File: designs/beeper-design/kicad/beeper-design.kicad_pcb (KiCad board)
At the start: 4 copper layers, 27.5 x 19 mm, 99 parts

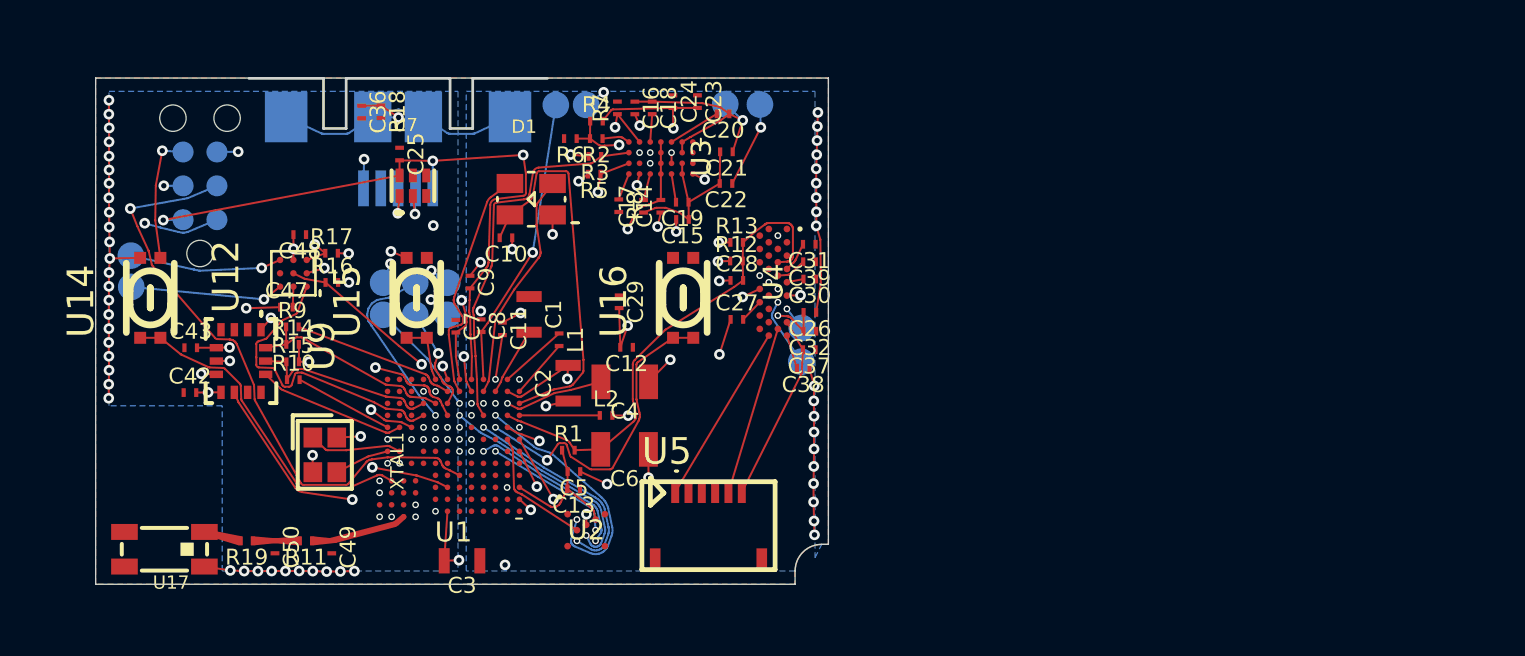
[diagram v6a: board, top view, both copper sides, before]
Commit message: exported, yet XTALM32p keeps disappearing
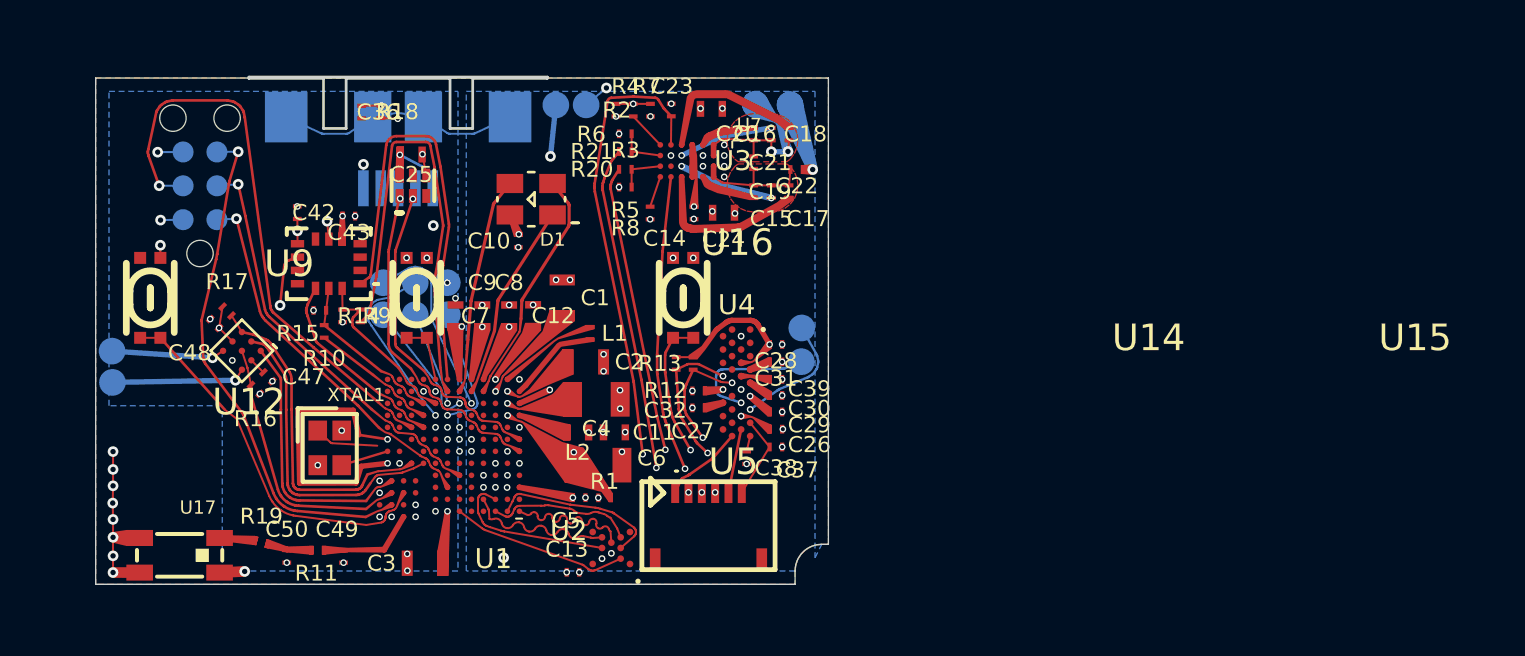
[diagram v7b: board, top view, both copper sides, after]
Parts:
- removed the C24 at (147.4, 99.4)
- removed the C6 at (145.6, 112.4)
- removed the D1 at (142.1, 103.0)
- removed the TP1 at (127.1, 106.3)
- added ?: , beeper-design:dummy9, F.Cu at (146.6, 100.4)
- added ?: , beeper-design:dummy10, F.Cu at (138.3, 110.6)
- added ?: , beeper-design:dummy11, F.Cu at (137.3, 109.6)
- added ?: , beeper-design:dummy12, F.Cu at (150.5, 109.8)
- added ?: , beeper-design:dummy13, F.Cu at (150.7, 110.2)
- added ?: , beeper-design:dummy14, F.Cu at (148.5, 100.5)
- added ?: , beeper-design:dummy15, F.Cu at (147.6, 100.7)
- added ?: , beeper-design:dummy16, F.Cu at (148.5, 101.6)
- added ?: , beeper-design:dummy17, F.Cu at (148.7, 102.7)
- added ?: , beeper-design:dummy18, F.Cu at (141.4, 112.4)
- added ?: , beeper-design:dummy19, F.Cu at (137.7, 109.6)
- added ?: , beeper-design:dummy20, F.Cu at (150.7, 109.3)
- added ?: , beeper-design:dummy21, F.Cu at (137.4, 113.0)
- added ?: , beeper-design:dummy22, F.Cu at (136.1, 113.3)
- added ?: , beeper-design:dummy23, F.Cu at (138.8, 113.6)
- added ?: , beeper-design:dummy24, F.Cu at (136.6, 111.7)
- added ?: , beeper-design:dummy25, F.Cu at (135.8, 116.2)
- added ?: , beeper-design:dummy26, F.Cu at (136.9, 115.6)
- added ?: , beeper-design:dummy27, F.Cu at (134.7, 116.2)
- added ?: , beeper-design:dummy28, F.Cu at (139.5, 109.3)
- added ?: , beeper-design:dummy29, F.Cu at (150.7, 99.7)
- added ?: , beeper-design:dummy30, F.Cu at (148.5, 100.0)
- added ?: , beeper-design:dummy31, F.Cu at (144.3, 116.8)
- added ?: , beeper-design:dummy32, F.Cu at (143.8, 114.4)
- added ?: , beeper-design:dummy33, F.Cu at (144.5, 114.4)
- added ?: , beeper-design:dummy34, F.Cu at (143.8, 115.6)
- added ?: , beeper-design:dummy35, F.Cu at (142.6, 114.1)
- added ?: , beeper-design:dummy36, F.Cu at (149.7, 102.7)
- added ?: , beeper-design:dummy37, F.Cu at (148.6, 102.4)
- added ?: , beeper-design:dummy38, F.Cu at (142.6, 111.6)
- added ?: , beeper-design:dummy39, F.Cu at (136.6, 110.4)
- added ?: , beeper-design:dummy40, F.Cu at (137.8, 111.5)
- added ?: , beeper-design:dummy41, F.Cu at (139.2, 113.3)
- added ?: , beeper-design:dummy42, F.Cu at (136.3, 111.1)
- added ?: , beeper-design:dummy43, F.Cu at (138.2, 109.7)
- added ?: , beeper-design:dummy44, F.Cu at (141.4, 112.0)
- added ?: , beeper-design:dummy45, F.Cu at (140.3, 109.2)
- added ?: , beeper-design:dummy46, F.Cu at (138.9, 109.8)
- added ?: , beeper-design:dummy47, F.Cu at (150.9, 103.6)
- added ?: , beeper-design:dummy49, F.Cu at (131.1, 115.8)
- added ?: , beeper-design:dummy50, F.Cu at (133.4, 116.2)
- added ?: , beeper-design:dummy51, F.Cu at (132.6, 116.1)
- added ?: , beeper-design:dummy52, F.Cu at (141.5, 104.0)
- added ?: , beeper-design:dummy53, F.Cu at (142.2, 110.4)
- added ?: , beeper-design:dummy54, F.Cu at (137.8, 111.1)
- added ?: , beeper-design:dummy55, F.Cu at (136.4, 109.8)
- added ?: , beeper-design:dummy56, F.Cu at (141.3, 110.8)
- added ?: , beeper-design:dummy57, F.Cu at (142.8, 110.6)
- added ?: , beeper-design:dummy58, F.Cu at (135.0, 104.2)
- added ?: , beeper-design:dummy59, F.Cu at (141.4, 111.2)
- added ?: , beeper-design:dummy61, F.Cu at (150.5, 108.8)
- added ?: , beeper-design:dummy62, F.Cu at (148.6, 108.5)
- added ?: , beeper-design:dummy63, F.Cu at (144.3, 113.4)
- added ?: , beeper-design:dummy64, F.Cu at (151.0, 100.2)
- added ?: , beeper-design:dummy66, F.Cu at (141.5, 108.8)
- added ?: , beeper-design:dummy67, F.Cu at (150.7, 110.8)
- added ?: , beeper-design:dummy68, F.Cu at (148.2, 102.2)
- added ?: , beeper-design:dummy6, F.Cu at (136.1, 114.5)
- added ?: , beeper-design:dummy69, F.Cu at (148.1, 101.6)
- added ?: , beeper-design:dummy71, F.Cu at (148.1, 102.0)
- added ?: , beeper-design:dummy72, F.Cu at (140.2, 108.8)
- added ?: , beeper-design:dummy73, F.Cu at (148.1, 101.2)
- added ?: , beeper-design:dummy74, F.Cu at (142.8, 108.8)
- added ?: , beeper-design:dummy75, F.Cu at (127.1, 115.8)
- added ?: , beeper-design:dummy76, F.Cu at (152.1, 100.6)
- added ?: , beeper-design:dummy77, F.Cu at (152.5, 101.9)
- added ?: , beeper-design:dummy78, F.Cu at (149.6, 110.7)
- added ?: , beeper-design:dummy7, F.Cu at (149.9, 100.5)
- added ?: , beeper-design:dummy80, F.Cu at (139.3, 108.8)
- added ?: , beeper-design:dummy81, F.Cu at (150.5, 111.5)
- added ?: , beeper-design:dummy82, F.Cu at (143.1, 109.2)
- added ?: , beeper-design:dummy83, F.Cu at (136.7, 113.7)
- added ?: , beeper-design:dummy84, F.Cu at (136.1, 114.1)
- added ?: , beeper-design:dummy85, F.Cu at (140.8, 110.0)
- added ?: , beeper-design:dummy86, F.Cu at (142.4, 108.5)
- added ?: , beeper-design:dummy87, F.Cu at (137.2, 114.3)
- added ?: , beeper-design:dummy8, F.Cu at (148.6, 100.8)
- added ?: , beeper-design:dummy89, F.Cu at (141.3, 110.3)
- added ?: , beeper-design:dummy90, F.Cu at (142.7, 109.6)
- added ?: , beeper-design:dummy91, F.Cu at (138.8, 115.9)
- added ?: , beeper-design:dummy92, F.Cu at (136.4, 114.7)
- added ?: , beeper-design:dummy93, F.Cu at (149.4, 102.4)
- added ?: , beeper-design:dummy94, F.Cu at (140.4, 110.1)
- added ?: , beeper-design:dummy95, F.Cu at (141.7, 107.7)
- added ?: , beeper-design:dummy96, F.Cu at (149.0, 110.8)
- added ?: , beeper-design:dummy98, F.Cu at (140.9, 108.8)
- added C1: 22u, beeper-design:Pkg0603, F.Cu at (143.3, 106.7)
- added C2: 22u, beeper-design:Pkg0603_1, F.Cu at (144.1, 109.2)
- added C37: 1u, beeper-design:Pkg0201_18, F.Cu at (151.3, 112.3)
- added C48: 1u, beeper-design:Pkg0201_33, F.Cu at (130.2, 107.7)
- added R16: 8K2, beeper-design:Pkg0201_40, F.Cu at (131.7, 110.2)
- added R20: 0R, beeper-design:Pkg0201, F.Cu at (145.6, 101.9)
- added R21: 0R, beeper-design:Pkg0201_8, F.Cu at (145.6, 101.3)
- added R7: 10K, beeper-design:Pkg0201_12, F.Cu at (147.4, 99.7)
- added R8: 1K, beeper-design:Pkg0201_16, F.Cu at (146.6, 103.6)
- added TP5: ~, beeper-design:SMD_TESTPT, B.Cu at (136.5, 106.2)
- added TP6: ~, beeper-design:SMD_TESTPT, B.Cu at (137.7, 106.2)
- added U16: ~, beeper-design:LP_2, F.Cu at (147.8, 106.8)
- added U2: ~, beeper-design:WLCSP_12, F.Cu at (145.1, 116.1)
- ?: renamed from U2; value ~ -> (none); footprint beeper-design:WLCSP_12 -> beeper-design:dummy48
- ?: renamed from TP6; value ~ -> (none); footprint beeper-design:SMD_TESTPT -> beeper-design:dummy60; moved to F.Cu
- ?: renamed from TP5; value ~ -> (none); footprint beeper-design:SMD_TESTPT -> beeper-design:dummy65; moved to F.Cu
- ?: renamed from R16; value 8K2 -> (none); footprint beeper-design:Pkg0201_31 -> beeper-design:dummy70
- ?: renamed from R7; value 10K -> (none); footprint beeper-design:Pkg0201_23 -> beeper-design:dummy79
- ?: renamed from C2; value 22u -> (none); footprint beeper-design:Pkg0603_1 -> beeper-design:dummy88
- ?: renamed from C37; value 2.2u -> (none); footprint beeper-design:Pkg0201_39 -> beeper-design:dummy97
- C10: footprint beeper-design:Pkg0201_12 -> beeper-design:Pkg0201_27
- C11: value 2.2u -> 10u; footprint beeper-design:Pkg0201_5 -> beeper-design:Pkg0402_6
- C12: value 2.2u -> 10u; footprint beeper-design:Pkg0201_25 -> beeper-design:Pkg0402_5
- C13: value 2.2u -> 1u; footprint beeper-design:Pkg0201_28 -> beeper-design:Pkg0201_29
- C14: footprint beeper-design:Pkg0201 -> beeper-design:Pkg0201_20
- C15: value 2.2u -> 470n; footprint beeper-design:Pkg0201_50 -> beeper-design:Pkg0201_23
- C16: value 2.2u -> 470n; footprint beeper-design:Pkg0201_9 -> beeper-design:Pkg0201_30
- C17: value 2.2u -> 22n; footprint beeper-design:Pkg0201_22 -> beeper-design:Pkg0201_36
- C18: value 2.2u -> 22n; footprint beeper-design:Pkg0201_36 -> beeper-design:Pkg0201_44
- C19: value 2.2u -> 10n; footprint beeper-design:Pkg0201_49 -> beeper-design:Pkg0201_2
- C20: value 2.2u -> 10n; footprint beeper-design:Pkg0201_7 -> beeper-design:Pkg0201_11
- C21: value 2.2u -> 270p; footprint beeper-design:Pkg0201_20 -> beeper-design:Pkg0201_17
- C22: value 2.2u -> 10n; footprint beeper-design:Pkg0201_33 -> beeper-design:Pkg0201_22
- C23: value 2.2u -> 10u; footprint beeper-design:Pkg0201_48 -> beeper-design:Pkg0402_4
- C24: renamed from C1; value 22u -> 4.7u; footprint beeper-design:Pkg0603 -> beeper-design:Pkg0402_7
- C25: value 2.2u -> 4.7u; footprint beeper-design:Pkg0201_18 -> beeper-design:Pkg0402_8
- C26: value 2.2u -> 1u; footprint beeper-design:Pkg0201_34 -> beeper-design:Pkg0201_43
- C27: value 2.2u -> 100n; footprint beeper-design:Pkg0201_53 -> beeper-design:Pkg0201_46
- C28: value 2.2u -> 1u; footprint beeper-design:Pkg0201_42 -> beeper-design:Pkg0201_38
- C29: value 2.2u -> 1u; footprint beeper-design:Pkg0201_24 -> beeper-design:Pkg0201_13
- C30: value 2.2u -> 1u; footprint beeper-design:Pkg0201_8 -> beeper-design:Pkg0201_31
- C31: value 2.2u -> 1u; footprint beeper-design:Pkg0201_21 -> beeper-design:Pkg0201_35
- C32: value 2.2u -> 1u; footprint beeper-design:Pkg0201_11 -> beeper-design:Pkg0201_6
- C36: value 2.2u -> 100n; footprint beeper-design:Pkg0201_30 -> beeper-design:Pkg0201_7
- C38: value 2.2u -> 1u; footprint beeper-design:Pkg0201_51 -> beeper-design:Pkg0201_24
- C39: value 2.2u -> 1u; footprint beeper-design:Pkg0201_47 -> beeper-design:Pkg0201_1
- C42: value 2.2u -> 100n; footprint beeper-design:Pkg0201_43 -> beeper-design:Pkg0201_34
- C43: value 2.2u -> 100n; footprint beeper-design:Pkg0201_3 -> beeper-design:Pkg0201_41
- C47: value 2.2u -> 1u; footprint beeper-design:Pkg0201_4 -> beeper-design:Pkg0201_26
- C49: value 2.2u -> 1p; footprint beeper-design:Pkg0201_37 -> beeper-design:Pkg0201_5
- C5: value 2.2u -> 100n; footprint beeper-design:Pkg0201_1 -> beeper-design:Pkg0201_39
- C50: value 2.2u -> 1p; footprint beeper-design:Pkg0201_2 -> beeper-design:Pkg0201_15
- C6: renamed from R8; value 1K -> 47u; footprint beeper-design:Pkg0201_38 -> beeper-design:Pkg0805
- C7: value 2.2u -> 10u; footprint beeper-design:Pkg0201_26 -> beeper-design:Pkg0402
- C8: value 2.2u -> 10u; footprint beeper-design:Pkg0201_41 -> beeper-design:Pkg0402_1
- C9: value 2.2u -> 10u; footprint beeper-design:Pkg0201_54 -> beeper-design:Pkg0402_2
- D1: renamed from C48; value 2.2u -> ~; footprint beeper-design:Pkg0201_16 -> beeper-design:LP_5
- L1: footprint beeper-design:Pkg0201_32 -> beeper-design:Pkg0201_21
- L2: value 470n -> 1u; footprint beeper-design:Pkg0201_46 -> beeper-design:Pkg0402_3
- R1: footprint beeper-design:Pkg0201_19 -> beeper-design:Pkg0201_14
- R10: footprint beeper-design:Pkg0201_44 -> beeper-design:Pkg0201_9
- R11: footprint beeper-design:Pkg0201_45 -> beeper-design:Pkg0201_10
- R12, R13: footprint beeper-design:Pkg0201_29 -> beeper-design:Pkg0201_28
- R14, R15: footprint beeper-design:Pkg0201_14 -> beeper-design:Pkg0201_42
- R17: footprint beeper-design:Pkg0201_31 -> beeper-design:Pkg0201_40
- R18: footprint beeper-design:Pkg0201_17 -> beeper-design:Pkg0201_47
- R19: footprint beeper-design:Pkg0201_13 -> beeper-design:Pkg0201_19
- R2: footprint beeper-design:Pkg0201_15 -> beeper-design:Pkg0201_25
- R3: footprint beeper-design:Pkg0201_10 -> beeper-design:Pkg0201_4
- R4: footprint beeper-design:Pkg0201_40 -> beeper-design:Pkg0201_37
- R5: footprint beeper-design:Pkg0201_52 -> beeper-design:Pkg0201_45
- R6: footprint beeper-design:Pkg0201_27 -> beeper-design:Pkg0201_32
- R9: footprint beeper-design:Pkg0201_35 -> beeper-design:Pkg0201_3
- TP1: renamed from U16; footprint beeper-design:LP_2 -> beeper-design:SMD_TESTPT; moved to B.Cu
- moved TP1 21.7 mm to (126.4, 109.9), turned to 180 degrees
- moved ? 20.2 mm to (148.9, 102.0)
- moved ? 13.4 mm to (148.9, 101.2), turned to 0 degrees
- moved ? 13.0 mm to (147.8, 103.0)
- moved ? 11.5 mm to (141.1, 107.5), turned to 0 degrees
- moved ? 11.2 mm to (149.0, 110.2), turned to 0 degrees
- moved C6 9.77 mm to (144.6, 113.0), turned to 270 degrees
- moved ? 9.02 mm to (136.2, 115.2), turned to 0 degrees
- moved ? 8.95 mm to (137.8, 110.6)
- moved D1 8.79 mm to (142.1, 103.0), turned to 0 degrees
- moved C24 8.24 mm to (149.3, 103.6), turned to 270 degrees
- moved ? 8.17 mm to (142.9, 112.5), turned to 0 degrees
- moved C42 7.86 mm to (133.3, 103.6), turned to 0 degrees
- moved ? 7.76 mm to (136.6, 109.6)
- moved C43 7.72 mm to (135.3, 103.7), turned to 270 degrees
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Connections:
- net board-io_qsen-i3c_sda renamed mcu_sda2
- net codec-pdm-net_clk renamed board-io_clk
- net codec-pdm-net_data renamed board-io_data
- net mcu_mcu-button1_gpio renamed mcu1_gpio1
- net mcu_mcu-dbg-m33_swdclk renamed mcu_swdclk
- net mcu_mcu-dbg-m33_swdio renamed mcu_swdio
- net mcu_mcu-etm_data1 renamed mcu_data1
- net mcu_mcu-etm_data2 renamed mcu_data2
- net mcu_mcu-etm_data3 renamed mcu_data3
- net mcu_q-spi_sdo renamed mcu_sdo
- C24 pad 2: V12 -> RECT
- C3 pad 2: V14 -> V14RF
- C6 pad 1: AD -> GND
- C6 pad 2: GND -> VDD1P8P
- D1 pad 1: GND -> board-io_r
- D1 pad 2: VDDSYS -> VLED
- J1 pad 3: mcu_conn-uart_rx -> mcu_rx
- J1 pad 6: mcu_mcu-uart_tx -> mcu_tx
- R10 pad 1: board-io_qsen-i3c_scl -> mcu_scl
- R10 pad 2: mcu_q-spi_sck -> mcu_sck
- R12 pad 1: codec-i2c-net_sda -> mcu_sda
- R13 pad 1: codec-i2c-net_scl -> mcu_scl2
- R15 pad 1: board-io_qsen-i3c_scl -> mcu_scl
- R17 pad 1: mcu_hap-i2c_scl -> mcu_scl1
- R3 pad 1: mcu_mcu-wpwr1_gpio -> EN2
- R5 pad 1: mcu_mcu-wpwr0_gpio -> EN1
- U1 pad A1: (no net) -> mcu_sdio0
- U1 pad A2: (no net) -> mcu_sdio1
- U1 pad A3: (no net) -> mcu_sdio2
- U1 pad A6: (no net) -> mcu_cs1
- U1 pad A7: V14 -> V14RF
- U1 pad B1: codec-i2c-net_scl -> (no net)
- U1 pad B11: (no net) -> mcu_tx
- U1 pad B3: (no net) -> mcu_sdio3
- U1 pad B4: (no net) -> mcu_sck1
- U1 pad C10: (no net) -> mcu0_gpio1
- U1 pad C11: (no net) -> mcu_sda1
- U1 pad C3: (no net) -> mcu_scl2
- U1 pad C4: (no net) -> mcu2_gpio1
- U1 pad D11: mcu_mcu-button0_gpio -> mcu0_gpio
- U1 pad D2: (no net) -> mcu2_gpio
- U1 pad D4: (no net) -> mcu_sda
- U1 pad E1: (no net) -> mcu1_gpio2
- U1 pad E10: (no net) -> mcu_scl1
- U1 pad E3: (no net) -> mcu0_gpio2
- U1 pad E9: (no net) -> mcu1_gpio
- U1 pad F2: (no net) -> mcu3_gpio
- U1 pad F3: mcu_mcu-mem_sdio3 -> (no net)
- U1 pad F4: mcu_mcu-mem_sck -> (no net)
- U1 pad G10: mcu_hap-i2c_scl -> (no net)
- U1 pad G2: mcu_mcu-mem_sdio1 -> (no net)
- U1 pad G8: mcu_conn-uart_rx -> (no net)
- U1 pad G9: mcu_mcu-uart_tx -> (no net)
- U1 pad H10: mcu_q-spi_sdi -> mcu_rx
- U1 pad H11: mcu_q-spi_cs -> (no net)
- U1 pad H12: mcu_q-spi_sck -> (no net)
- U1 pad H2: codec-i2c-net_sda -> (no net)
- U1 pad H3: mcu_mcu-button2_gpio -> (no net)
- U1 pad H4: mcu_mcu-mem_sdio2 -> (no net)
- U1 pad H9: mcu_hap-gpio1_gpio -> mcu_cs
- U1 pad J3: mcu_mcu-mem_cs -> (no net)
- U1 pad J4: mcu_mcu-wpwr1_gpio -> (no net)
- U1 pad J5: mcu_mcu-wpwr3_gpio -> (no net)
- U1 pad J6: mcu_mcu-mem_sdio0 -> (no net)
- U1 pad J8: mcu_mcu-etm_data0 -> mcu_data0
- U1 pad J9: mcu_hap-gpio0_gpio -> mcu_sck
- U1 pad K3: mcu_mcu-wpwr2_gpio -> (no net)
- U1 pad K4: mcu_mcu-wpwr0_gpio -> (no net)
- U1 pad K5: mcu_mcu-etm_clk -> mcu_clk
- U1 pad K9: board-io_qsen-i3c_scl -> mcu_scl
- U1 pad L2: V14 -> V14RF
- U1 pad L4: board-io_rgb_b -> board-io_b
- U1 pad L5: board-io_rgb_r -> board-io_r
- U1 pad L6: board-io_rgb_g -> board-io_g
- U1 pad M7: mcu_hap-i2c_sda -> mcu_sdi
- U12 pad A1: mcu_hap-gpio0_gpio -> mcu0_gpio
- U12 pad B1: mcu_hap-gpio1_gpio -> mcu1_gpio
- U12 pad B2: mcu_hap-i2c_sda -> mcu_sda1
- U12 pad C1: mcu_hap-i2c_scl -> mcu_scl1
- U14 pad A: mcu_mcu-button0_gpio -> mcu0_gpio1
- U14 pad A1: mcu_mcu-button0_gpio -> mcu0_gpio1
- U3 pad F1: mcu_mcu-wpwr3_gpio -> mcu3_gpio
- U3 pad F4: mcu_mcu-wpwr2_gpio -> mcu2_gpio1
- U3 pad G2: mcu_mcu-wpwr1_gpio -> EN2
- U3 pad G3: mcu_mcu-wpwr0_gpio -> EN1
- U4 pad C9: codec-i2c-net_sda -> mcu_sda
- U4 pad D8: codec-i2c-net_scl -> mcu_scl2
- U9 pad 1: mcu_q-spi_sdi -> mcu_sdi
- U9 pad 12: mcu_q-spi_cs -> mcu_cs
- U9 pad 13: board-io_qsen-i3c_scl -> mcu_scl
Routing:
- net GND: track 53.7 -> 25.5 mm, vias 101 -> 98
- net VDDSYS: track 6.88 -> 31.8 mm, vias 7 -> 6
- net mcu3_gpio: track 0.00 -> 22.5 mm, vias 0 -> 2
- net mcu_rx: track 0.00 -> 20.9 mm, vias 0 -> 1
- net mcu2_gpio1: track 0.00 -> 19.1 mm, vias 0 -> 2
- net mcu_tx: track 0.00 -> 18.2 mm, vias 0 -> 1
- net mcu0_gpio2: track 0.00 -> 17.9 mm, vias 0 -> 2
- net mcu1_gpio2: track 0.00 -> 17.4 mm, vias 0 -> 2
- net mcu_sdi: track 0.00 -> 16.5 mm
- net codec-i2c-net_scl: track 15.6 -> 0.00 mm, vias 3 -> 0
- net mcu_conn-uart_rx: track 15.2 -> 0.00 mm, vias 2 -> 0
- net VDD3P0: track 25.4 -> 10.9 mm
- net mcu_mcu-wpwr3_gpio: track 14.2 -> 0.00 mm, vias 2 -> 0
- net mcu_mcu-wpwr1_gpio: track 14.2 -> 0.00 mm
- net mcu_mcu-uart_tx: track 14.1 -> 0.00 mm, vias 2 -> 0
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- added copper zone on F.Cu, net AC1
- added copper zone on F.Cu, net AC2
- added copper zone on In2.Cu, net GND
- added copper zone on In2.Cu, net VBAT
- added copper zone on In2.Cu, net VBUS
- added copper zone on In2.Cu, net VDD1P8
- added copper zone on In2.Cu, net VDD1P8P
- added copper zone on In2.Cu, net VDD3P0
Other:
- net class BGA added: clearance 0.065, trace_width 0.075, via_dia 0.015, via_drill 0.15
- net class Default added: clearance 0.0625, trace_width 0.075, via_dia 0.015, via_drill 0.15
- net class RF added: clearance 0.0625, trace_width 0.221435, via_dia 0.015, via_drill 0.15
- rule pad_to_mask_clearance: 0 -> 0.051

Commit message: fixed up pours, keepout regions
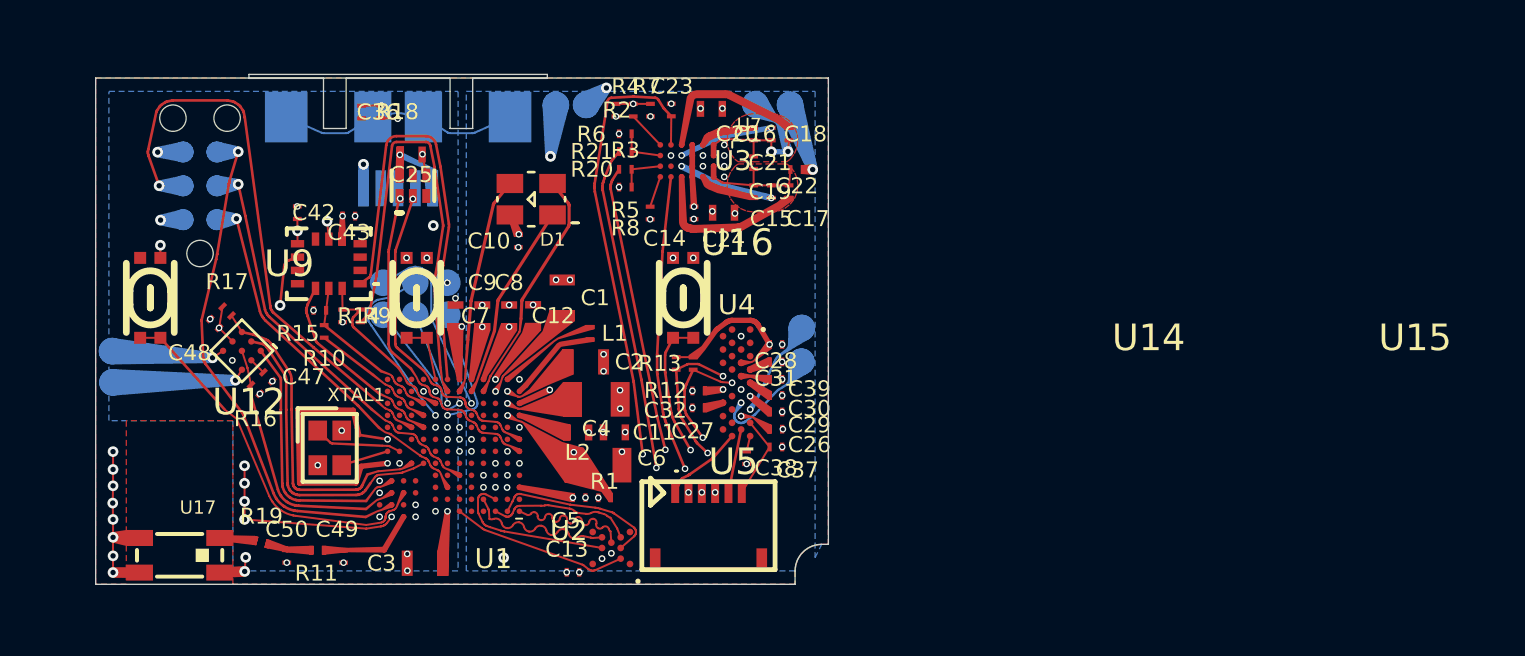
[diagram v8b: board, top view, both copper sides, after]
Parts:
- removed the ? at (148.5, 101.6)
- removed the ? at (143.8, 115.6)
- removed the ? at (139.2, 113.3)
- removed the ? at (133.4, 116.2)
- added ?: , beeper-design:dummy103, F.Cu at (136.4, 109.8)
- added ?: , beeper-design:dummy110, F.Cu at (148.6, 108.5)
- added ?: , beeper-design:dummy104, F.Cu at (141.3, 110.8)
- added ?: , beeper-design:dummy107, F.Cu at (141.4, 111.2)
- added ?: , beeper-design:dummy108, F.Cu at (142.9, 112.5)
- added ?: , beeper-design:dummy101, F.Cu at (151.5, 109.2)
- added ?: , beeper-design:dummy112, F.Cu at (151.0, 100.2)
- added ?: , beeper-design:dummy105, F.Cu at (142.8, 110.6)
- added ?: , beeper-design:dummy106, F.Cu at (135.0, 104.2)
- added ?: , beeper-design:dummy102, F.Cu at (137.8, 111.1)
- added ?: , beeper-design:dummy111, F.Cu at (144.3, 113.4)
- added ?: , beeper-design:dummy109, F.Cu at (150.5, 108.8)
- added ?: , beeper-design:dummy99, F.Cu at (141.5, 104.0)
- added ?: , beeper-design:dummy100, F.Cu at (142.2, 110.4)
- added ?: , beeper-design:dummy113, F.Cu at (148.9, 101.2)
- added C27: 100n, beeper-design:Pkg0201_12, F.Cu at (148.4, 110.9)
- added R13: 8K2, beeper-design:Pkg0201_42, F.Cu at (147.5, 109.2)
- added R14: 8K2, beeper-design:Pkg0201_8, F.Cu at (135.0, 107.4)
- added U3: ~, beeper-design:LP_1, F.Cu at (148.1, 101.6)
- ?: renamed from R13; value 8K2 -> (none); footprint beeper-design:Pkg0201_28 -> beeper-design:dummy34
- ?: renamed from C27; value 100n -> (none); footprint beeper-design:Pkg0201_46 -> beeper-design:dummy50
- ?: renamed from R14; value 8K2 -> (none); footprint beeper-design:Pkg0201_42 -> beeper-design:dummy41
- ?: renamed from U3; value ~ -> (none); footprint beeper-design:LP_6 -> beeper-design:dummy16
- C10: footprint beeper-design:Pkg0201_27 -> beeper-design:Pkg0201_41
- C11: footprint beeper-design:Pkg0402_6 -> beeper-design:Pkg0402_8
- C12: footprint beeper-design:Pkg0402_5 -> beeper-design:Pkg0402_7
- C13: footprint beeper-design:Pkg0201_29 -> beeper-design:Pkg0201_43
- C14: footprint beeper-design:Pkg0201_20 -> beeper-design:Pkg0201_34
- C15: footprint beeper-design:Pkg0201_23 -> beeper-design:Pkg0201_37
- C16: footprint beeper-design:Pkg0201_30 -> beeper-design:Pkg0201_44
- C17: footprint beeper-design:Pkg0201_36 -> beeper-design:Pkg0201_2
- C18: footprint beeper-design:Pkg0201_44 -> beeper-design:Pkg0201_10
- C19: footprint beeper-design:Pkg0201_2 -> beeper-design:Pkg0201_16
- C20: footprint beeper-design:Pkg0201_11 -> beeper-design:Pkg0201_25
- C21: footprint beeper-design:Pkg0201_17 -> beeper-design:Pkg0201_31
- C22: footprint beeper-design:Pkg0201_22 -> beeper-design:Pkg0201_36
- C23: footprint beeper-design:Pkg0402_4 -> beeper-design:Pkg0402_6
- C24: footprint beeper-design:Pkg0402_7 -> beeper-design:Pkg0402
- C25: footprint beeper-design:Pkg0402_8 -> beeper-design:Pkg0402_1
- C26: footprint beeper-design:Pkg0201_43 -> beeper-design:Pkg0201_9
- C28: footprint beeper-design:Pkg0201_38 -> beeper-design:Pkg0201_4
- C29: footprint beeper-design:Pkg0201_13 -> beeper-design:Pkg0201_27
- C30: footprint beeper-design:Pkg0201_31 -> beeper-design:Pkg0201_45
- C31: footprint beeper-design:Pkg0201_35 -> beeper-design:Pkg0201_1
- C32: footprint beeper-design:Pkg0201_6 -> beeper-design:Pkg0201_20
- C36: footprint beeper-design:Pkg0201_7 -> beeper-design:Pkg0201_21
- C37: footprint beeper-design:Pkg0201_18 -> beeper-design:Pkg0201_32
- C38: footprint beeper-design:Pkg0201_24 -> beeper-design:Pkg0201_38
- C39: footprint beeper-design:Pkg0201_1 -> beeper-design:Pkg0201_15
- C42: footprint beeper-design:Pkg0201_34 -> beeper-design:Pkg0201
- C43: footprint beeper-design:Pkg0201_41 -> beeper-design:Pkg0201_7
- C47: footprint beeper-design:Pkg0201_26 -> beeper-design:Pkg0201_40
- C48: footprint beeper-design:Pkg0201_33 -> beeper-design:Pkg0201_47
- C49: footprint beeper-design:Pkg0201_5 -> beeper-design:Pkg0201_19
- C5: footprint beeper-design:Pkg0201_39 -> beeper-design:Pkg0201_5
- C50: footprint beeper-design:Pkg0201_15 -> beeper-design:Pkg0201_29
- C7: footprint beeper-design:Pkg0402 -> beeper-design:Pkg0402_2
- C8: footprint beeper-design:Pkg0402_1 -> beeper-design:Pkg0402_3
- C9: footprint beeper-design:Pkg0402_2 -> beeper-design:Pkg0402_4
- D1: footprint beeper-design:LP_5 -> beeper-design:LP
- L1: footprint beeper-design:Pkg0201_21 -> beeper-design:Pkg0201_35
- L2: footprint beeper-design:Pkg0402_3 -> beeper-design:Pkg0402_5
- R1: footprint beeper-design:Pkg0201_14 -> beeper-design:Pkg0201_28
- R10: footprint beeper-design:Pkg0201_9 -> beeper-design:Pkg0201_23
- R11: footprint beeper-design:Pkg0201_10 -> beeper-design:Pkg0201_24
- R12: footprint beeper-design:Pkg0201_28 -> beeper-design:Pkg0201_42
- R15: footprint beeper-design:Pkg0201_42 -> beeper-design:Pkg0201_8
- R16, R17: footprint beeper-design:Pkg0201_40 -> beeper-design:Pkg0201_6
- R18: footprint beeper-design:Pkg0201_47 -> beeper-design:Pkg0201_13
- R19: footprint beeper-design:Pkg0201_19 -> beeper-design:Pkg0201_33
- R2: footprint beeper-design:Pkg0201_25 -> beeper-design:Pkg0201_39
- R20: footprint beeper-design:Pkg0201 -> beeper-design:Pkg0201_14
- R21: footprint beeper-design:Pkg0201_8 -> beeper-design:Pkg0201_22
- R3: footprint beeper-design:Pkg0201_4 -> beeper-design:Pkg0201_18
- R4: footprint beeper-design:Pkg0201_37 -> beeper-design:Pkg0201_3
- R5: footprint beeper-design:Pkg0201_45 -> beeper-design:Pkg0201_11
- R6: footprint beeper-design:Pkg0201_32 -> beeper-design:Pkg0201_46
- R7: footprint beeper-design:Pkg0201_12 -> beeper-design:Pkg0201_26
- R8: footprint beeper-design:Pkg0201_16 -> beeper-design:Pkg0201_30
- R9: footprint beeper-design:Pkg0201_3 -> beeper-design:Pkg0201_17
- U1: footprint beeper-design:LP -> beeper-design:LP_3
- U12: footprint beeper-design:LP_7 -> beeper-design:LP_2
- U14, U15, U16: footprint beeper-design:LP_2 -> beeper-design:LP_5
- U4: footprint beeper-design:LP_3 -> beeper-design:LP_6
- U5: footprint beeper-design:LP_4 -> beeper-design:LP_7
- U9: footprint beeper-design:LP_1 -> beeper-design:LP_4
- moved ? 26.6 mm to (148.5, 100.0)
- moved ? 26.3 mm to (127.1, 115.8)
- moved ? 24.3 mm to (149.9, 100.5)
- moved ? 22.0 mm to (128.5, 109.9)
- moved ? 21.0 mm to (146.6, 100.4)
- moved ? 19.8 mm to (136.1, 113.3)
- moved ? 18.6 mm to (131.1, 115.8)
- moved ? 18.6 mm to (130.6, 101.3)
- moved ? 18.6 mm to (130.6, 103.8)
- moved ? 18.0 mm to (144.3, 116.8)
- moved ? 17.8 mm to (136.6, 114.2)
- moved ? 17.6 mm to (136.9, 115.6)
- moved ? 17.0 mm to (148.1, 101.6)
- moved ? 16.8 mm to (135.8, 102.4)
- moved ? 16.5 mm to (148.6, 102.4)
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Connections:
- ? pad trace: mcu_scl1 -> LY
- ? pad trace: BOOT1 -> board-io_b
- ? pad trace: mcu_sda2 -> GND
- ? pad trace: V12 -> mcu_cs (x2)
- ? pad trace: board-io_b -> COMM1 (x2)
- ? pad trace: VBAT -> RF2 (x2)
- ? pad trace: VLED -> mcu_sda2 (x2)
- ? pad trace: mcu_tx -> board-io_r
- ? pad trace: VMID -> GND
- ? pad trace: VDD1P8P -> D+ (x2)
- ? pad trace: BOOT2 -> VBUS (x2)
- ? pad trace: VDD3P0 -> OUT+
- ? pad trace: mcu_cs -> VBAT (x2)
- ? pad trace: GND -> COMM2
- ? pad trace: mcu0_gpio -> LZ
- ? pad trace: V14RF -> D- (x2)
- ? pad trace: V18F -> V14RF
- ? pad trace: LY -> BOOT1
- ? pad trace: D+ -> VDD3P0 (x2)
- ? pad trace: mcu_scl -> VBUS (x2)
- ? pad trace: VDD3P0 -> V18F (x3)
- ? pad trace: D- -> mcu_rx
- ? pad trace: V18F -> mcu_tx (x2)
- ? pad trace: mcu0_gpio1 -> mcu_swdclk (x2)
- ? pad trace: mcu_scl1 -> OUT-
- ? pad trace: VBUS -> board-io_g
- ? pad trace: mcu_sda1 -> VBUS (x2)
- ? pad trace: mcu_rx -> VDDSYS (x2)
- ? pad trace: mcu_sdo -> mcu_scl
- ? pad trace: VDDSYS -> mcu_swdio (x2)
- ? pad trace: mcu_sda2 -> LX
- ? pad trace: AC1 -> VBUS
- ? pad trace: VDD1P8P -> DACREF
- ? pad trace: mcu_swdio -> mcu0_gpio (x2)
- ? pad trace: VREF -> GND
- ? pad trace: mcu_swdclk -> mcu_rx
- ? pad trace: VDD1P8 -> RECT (x3)
- ? pad trace: COMM1 -> mcu_sda1 (x2)
- ? pad trace: FOD -> VBUS
- ? pad trace: cap_p1 -> V18F (x2)
- ? pad trace: V18F -> board-io_b
- ? pad trace: RF1 -> V12 (x2)
- ? pad trace: VDIG -> RF3
- ? pad trace: D- -> AC1
- ? pad trace: AC2 -> mcu_swdio
- ? pad trace: VBUS -> SP_P (x2)
- ? pad trace: RECT -> cap_p1
- ? pad trace: mcu0_gpio -> BOOT1
- ? pad trace: VBUS -> RF1 (x3)
- ? pad trace: VDD1P8P -> RECT
- ? pad trace: board-io_r -> mcu_scl
- ? pad trace: LZ -> VBAT
- ? pad trace: VDD1P8P -> mcu_scl1
- ? pad trace: DACREF -> VDD3P0
- ? pad trace: RF1 -> mcu0_gpio1
- ? pad trace: board-io_g -> mcu0_gpio1
- ? pad trace: CLAMP1 -> mcu_sdo
- ? pad trace: RECT -> VDD3P0
- ? pad trace: LX -> COMM2
- ? pad trace: mcu_sck -> VREF
- ? pad trace: AC2 -> mcu_scl1
- ? pad trace: V14RF -> mcu_swdclk
- ? pad trace: RF2 -> FOD
- ? pad trace: RF3 -> BOOT2
- ? pad trace: RECT -> GND
- ? pad trace: COMM2 -> V14RF (x2)
- ? pad trace: mcu_sck -> VMID
- ? pad trace: BOOT1 -> VDIG
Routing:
- net GND: track 25.5 -> 39.4 mm, vias 98 -> 103
- net SP_N: track 4.65 -> 0.00 mm
- net OUT+: track 5.08 -> 0.46 mm
- net SP_P: track 5.02 -> 1.16 mm
- net OUT-: track 4.25 -> 0.47 mm
- net VBUS: track 31.5 -> 28.8 mm
- net VBAT: track 8.11 -> 6.17 mm
- net mcu_rx: track 20.9 -> 20.0 mm
- net XTAL32Mp: track 2.42 -> 3.31 mm
- net mcu_swdclk: track 14.2 -> 13.4 mm
- net mcu_tx: track 18.2 -> 17.4 mm
- net mcu_swdio: track 13.0 -> 12.3 mm
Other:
- board size 27.5 x 19 mm -> 27.5 x 19.1 mm
- net class BGA removed
- net class Default removed
- net class RF removed
